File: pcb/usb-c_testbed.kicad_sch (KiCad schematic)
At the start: 8 parts, among them J3 USB_C_Receptacle_USB2.0_16P, U2 USBLC6-2SC6

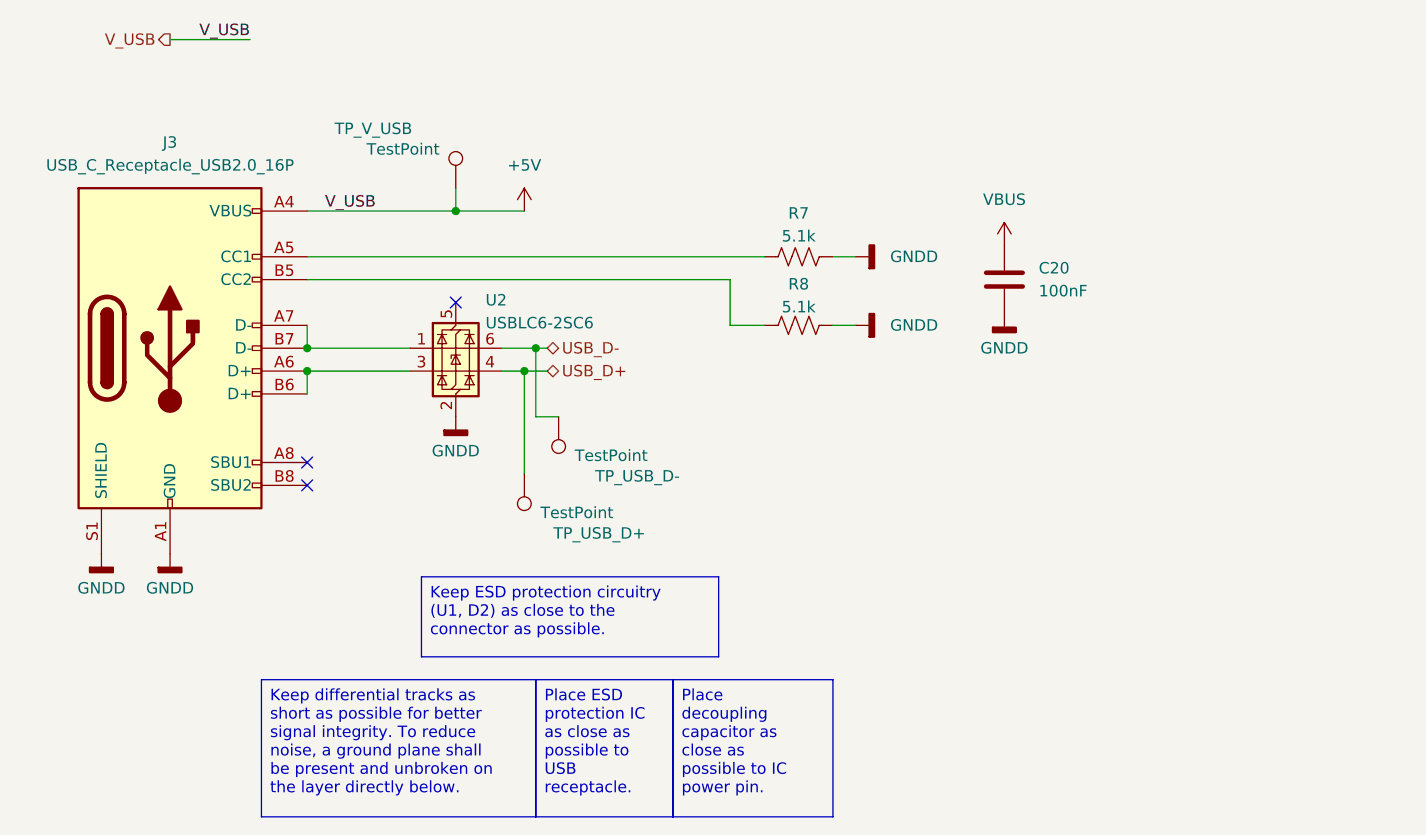
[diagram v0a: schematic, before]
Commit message: Updated Control Module Test bed schematics
Added Test points for Pyro controllers, Micro SD, and USB-C

Connected VDDUSB to 3.3V and not Vusb
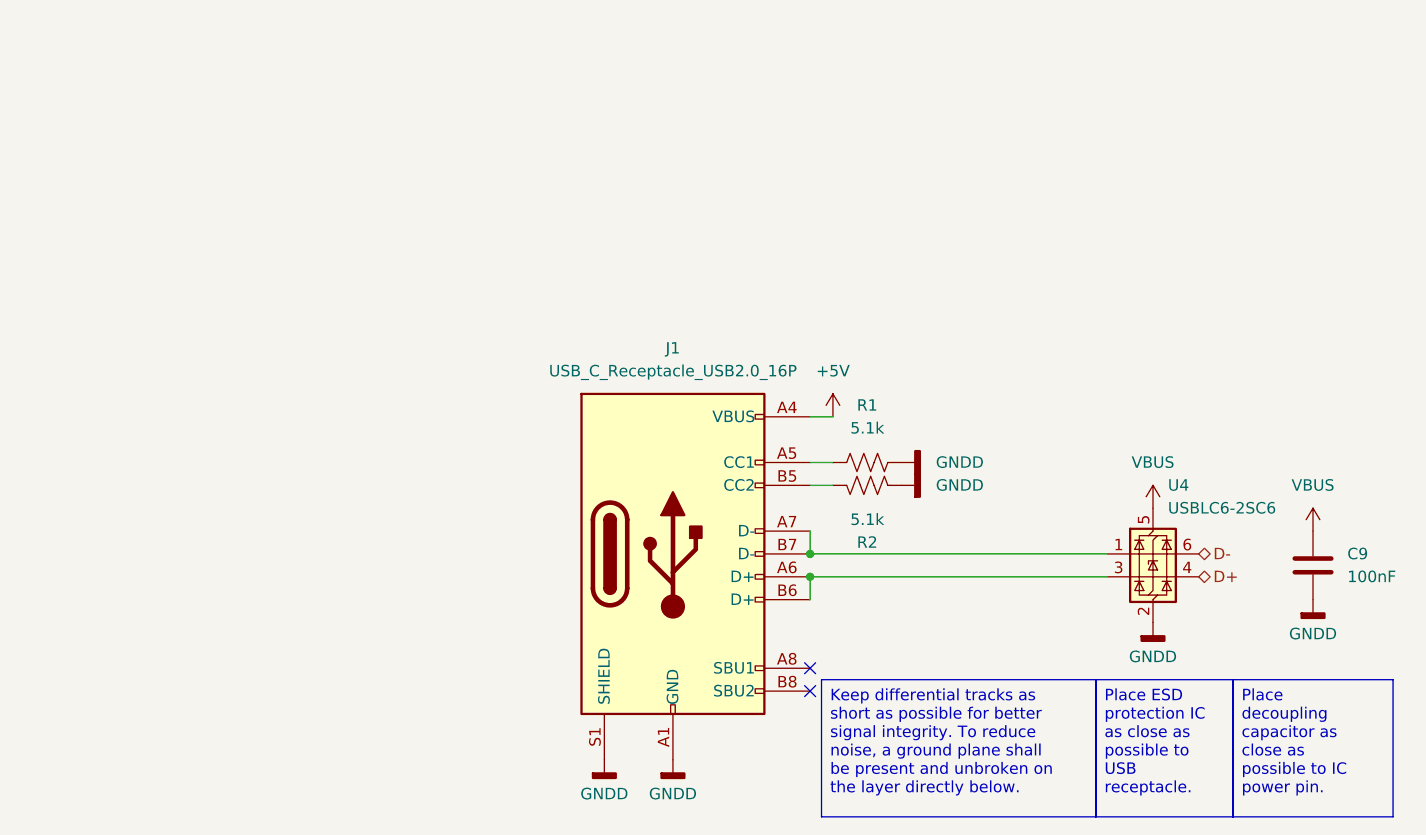
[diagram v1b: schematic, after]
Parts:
- removed C20: 100nF, Capacitor_SMD:C_0603_1608Metric_Pad1.08x0.95mm_HandSolder, symbol Device:C
- removed J3: USB_C_Receptacle_USB2.0_16P, Connector_USB:USB_C_Receptacle_GCT_USB4105-xx-A_16P_TopMnt_Horizontal, symbol Connector:USB_C_Receptacle_USB2.0_16P
- removed R7, R8: 5.1k, Resistor_SMD:R_0603_1608Metric, symbol Device:R_US
- removed TP_USB_D+, TP_USB_D-, TP_V_USB: TestPoint, TestPoint:TestPoint_Loop_D2.54mm_Drill1.5mm_Beaded, symbol Connector:TestPoint
- removed U2: USBLC6-2SC6, Package_TO_SOT_SMD:SOT-23-6, symbol Power_Protection:USBLC6-2SC6
- added C9: 100nF, Capacitor_SMD:C_0603_1608Metric_Pad1.08x0.95mm_HandSolder, symbol Device:C
- added J1: USB_C_Receptacle_USB2.0_16P, Connector_USB:USB_C_Receptacle_GCT_USB4105-xx-A_16P_TopMnt_Horizontal, symbol Connector:USB_C_Receptacle_USB2.0_16P
- added R1, R2: 5.1k, Resistor_SMD:R_0603_1608Metric_Pad0.98x0.95mm_HandSolder, symbol Device:R_US
- added U4: USBLC6-2SC6, Package_TO_SOT_SMD:SOT-23-6, symbol Power_Protection:USBLC6-2SC6
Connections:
- net +5V: now also J1.A4 (VBUS), J1.A9 (VBUS), J1.B4 (VBUS), J1.B9 (VBUS)
- net GNDD: now also C9.2, J1.A1 (GND), J1.A12 (GND), J1.B1 (GND), J1.B12 (GND), J1.S1 (SHIELD), R1.2, R2.2, U4.2 (GND)
- net VBUS: now also C9.1, U4.5 (VBUS)
- new net: J1.A5 (CC1), R1.1
- new net: J1.A6 (D+), J1.B6 (D+), U4.3 (I/O2)
- new net: J1.A7 (D-), J1.B7 (D-), U4.1 (I/O1)
- new net: J1.B5 (CC2), R2.1
- new net D+: U4.4 (I/O2)
- new net D-: U4.6 (I/O1)
- no-connect marks 3 -> 2
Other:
- company: Rowan Rocketry -> Dynamite Rocketry
- title: Ride-Along Module -> USB-C Interface
